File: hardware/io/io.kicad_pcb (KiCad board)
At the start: 4 copper layers, 215 x 232 mm, 793 parts, among them J1 USB_B, J10 Conn_02x18_Odd_Even, J11 Barrel_Jack_Switch_Pin3Ring, J2 Conn_02x03_Odd_Even, J3 Conn_02x08_Odd_Even, J4 Conn_02x40_Odd_Even, J5 Conn_02x16_Odd_Even, J6 Conn_02x16_Odd_Even, J7 Conn_02x12_Odd_Even, J8 Conn_02x24_Odd_Even, Q129 IRLML6244, Q130 IRLML6402, Q131 IRLML6244, Q132 IRLML6402, Q133 IRLML6244, Q134 IRLML6402, Q135 IRLML6244, Q136 IRLML6402, Q137 IRLML6244, Q138 IRLML6402, Q139 IRLML6244, Q140 IRLML6402, Q141 IRLML6244, Q142 IRLML6402, Q143 IRLML6244, Q144 IRLML6402, Q145 IRLML6244, Q146 IRLML6402, Q147 IRLML6244, Q148 IRLML6402, Q149 IRLML6244, Q150 IRLML6402, Q151 IRLML6244, Q152 IRLML6402, Q153 IRLML6244, Q154 IRLML6402, Q155 IRLML6244, Q156 IRLML6402, Q157 IRLML6244, Q158 IRLML6402, Q159 IRLML6244, Q160 IRLML6402, Q161 IRLML6244, Q162 IRLML6402, Q163 IRLML6244, Q164 IRLML6402, Q165 IRLML6244, Q166 IRLML6402, Q167 IRLML6244, Q168 IRLML6402, Q169 IRLML6244, Q170 IRLML6402, Q171 IRLML6244, Q172 IRLML6402, Q173 IRLML6244, Q174 IRLML6402, Q175 IRLML6244, Q176 IRLML6402, Q177 IRLML6244, Q178 IRLML6402, Q179 IRLML6244, Q180 IRLML6402, Q181 IRLML6244, Q182 IRLML6402, Q183 IRLML6244, Q184 IRLML6402, Q185 IRLML6244, Q186 IRLML6402, Q187 IRLML6244, Q188 IRLML6402, Q189 IRLML6244, Q190 IRLML6402, Q191 IRLML6244, Q192 IRLML6402, Q193 IRLML6244, Q194 IRLML6402, Q195 IRLML6244, Q196 IRLML6402, Q197 IRLML6244, Q198 IRLML6402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

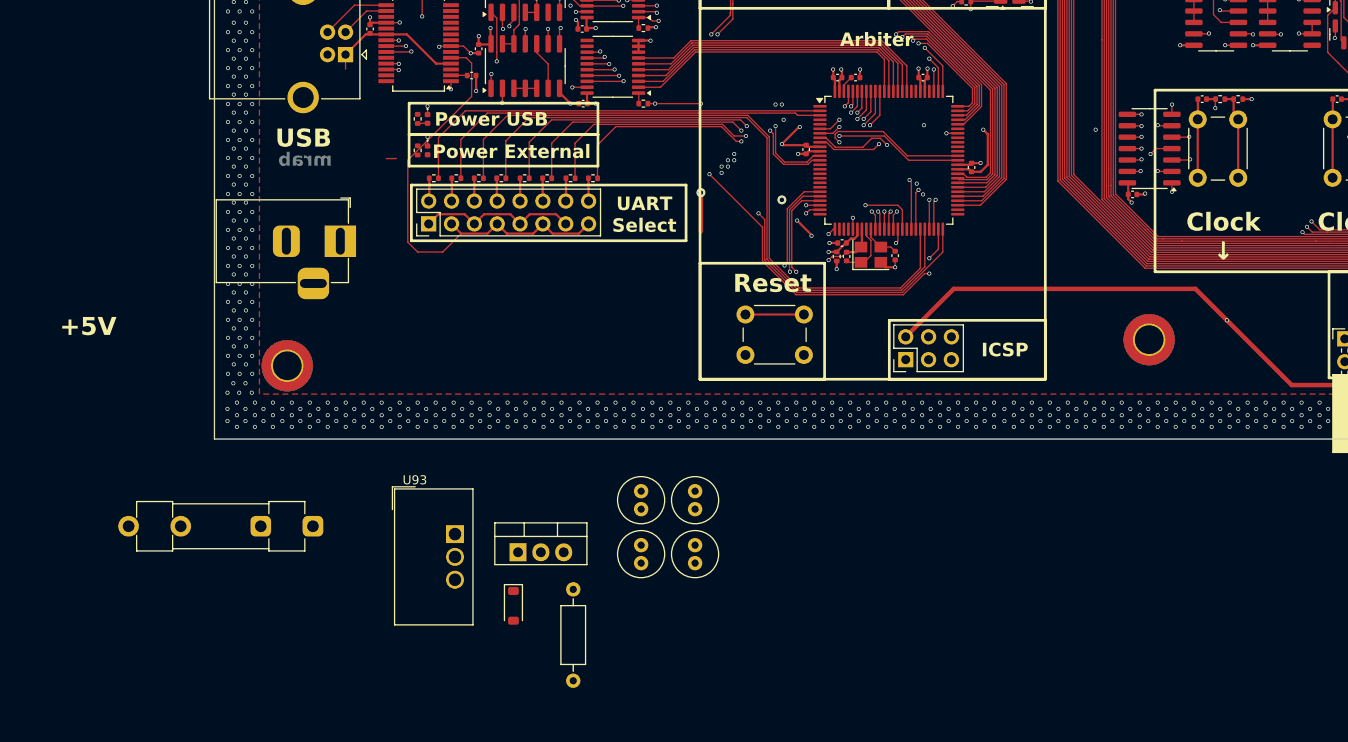
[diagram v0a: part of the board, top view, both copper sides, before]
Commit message: all PCBs passing all CRC & vibe checks
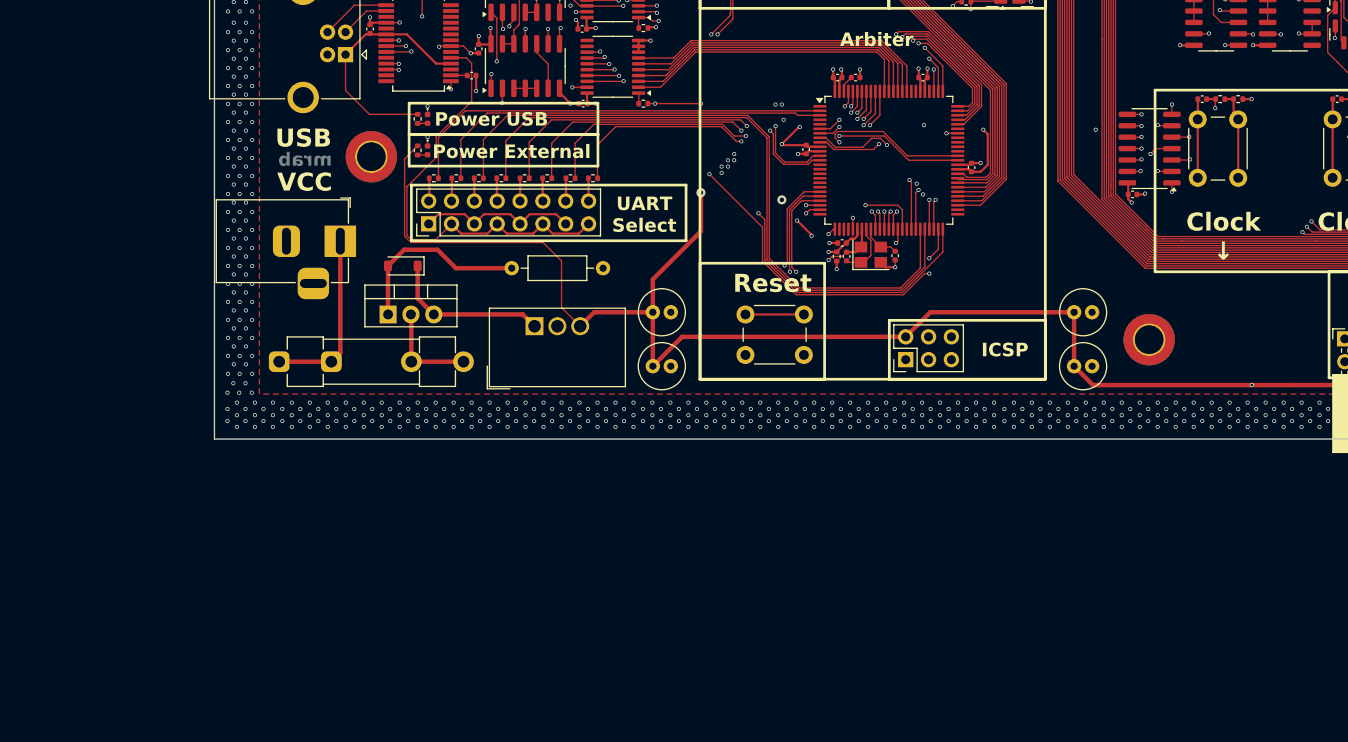
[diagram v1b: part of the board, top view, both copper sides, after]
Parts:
- R142, R143, R144, R145, R146, R147, R148, R149, R150, R151, R152, R153, R154, R155, R156, R157, R158, R159, R160, R161, R162, R163, R164, R165, R166, R167, R168, R169, R170, R171, R172, R173, R174, R175, R176, R177, R178, R179, R180, R181, R182, R183, R184, R185, R186, R187, R188, R189, R190, R191, R192, R193, R194, R195, R196, R197, R198, R199, R200, R201, R202, R203, R204, R205, R206, R207, R208, R209, R210, R211, R212, R213, R214, R215, R216, R217, R218, R219, R220, R221, R222, R223, R224, R225, R226, R227, R228, R229, R230, R231, R232, R233, R234, R235, R236, R237, R238, R239, R240, R241, R242, R243, R244, R245, R246, R247, R248, R249, R250, R251, R252, R253, R254, R255, R256, R257, R258, R259, R260, R261, R262, R263, R264, R265, R266, R267, R268, R269, R270, R271, R272, R273, R274, R277, R278, R279, R280, R281, R282, R283, R284, R285, R286, R287, R288, R289, R290, R291, R292, R293, R294, R295, R296, R297, R298, R299, R300, R301, R302, R303, R304, R305, R306, R308, R309: value 1000 -> 1K
- moved C97 52.1 mm to (312.6, 481.9), turned to 0 degrees
- moved C26 49.5 mm to (312.6, 475.9), turned to 0 degrees
- moved R115 46.4 mm to (250.1, 471.0), turned to 0 degrees
- moved D6 39.8 mm to (237.9, 470.8), turned to 180 degrees
- moved Q2 30.1 mm to (236.3, 476.1)
- moved H7 25.1 mm to (234.4, 458.6)
- moved U93 24.8 mm to (252.6, 477.5), turned to 90 degrees
- moved C98 21.9 mm to (265.8, 475.9), turned to 0 degrees
- moved F1 18.7 mm to (224.2, 481.4), turned to 0 degrees
- moved C41 16.6 mm to (265.8, 481.9), turned to 0 degrees
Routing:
- net +5V: track 3294.6 -> 3394.8 mm
- net Net-(D6-A): track 0.00 -> 20.8 mm
- net Net-(F1-Pad1): track 0.00 -> 19.6 mm
- net Net-(D6-K): track 0.00 -> 17.9 mm
- net VUSB: track 35.9 -> 47.3 mm
- net Net-(Q2-D): track 0.00 -> 11.1 mm
- net Net-(J3-Pin_11): track 50.5 -> 48.5 mm
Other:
- board text removed: "+5V"
